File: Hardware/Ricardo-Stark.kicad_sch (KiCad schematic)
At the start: 54 parts, among them J1 RBUS, U1 ESP32-S3, Y1 R940000171

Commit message: updated sensors and other stuff
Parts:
- removed 3V3LED10: PURPLE_LED, LED_SMD:LED_0402_1005Metric, symbol Device:LED_Small
- removed 3V3LED2, 3V3LED3, 3V3LED4, 3V3LED8: BLUE_LED, LED_SMD:LED_0402_1005Metric, symbol Device:LED_Small
- removed 3V3LED5: ORANGE_LED, LED_SMD:LED_0402_1005Metric, symbol Device:LED_Small
- removed 3V3LED6: RED_LED, LED_SMD:LED_0402_1005Metric, symbol Device:LED_Small
- removed 3V3LED7: YELLOW_LED, LED_SMD:LED_0402_1005Metric, symbol Device:LED_Small
- removed 3V3LED9: GREEN_LED, LED_SMD:LED_0402_1005Metric, symbol Device:LED_Small
- removed JP31: SolderJumper_2_Open, iclr:SmallerSolderJP, symbol Jumper:SolderJumper_2_Open
- removed R11, R12, R13, R44: 470, Resistor_SMD:R_0402_1005Metric, symbol Device:R_Small
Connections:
- net GPIO37: no longer U1.42 (GPIO37)
- net GPIO38: no longer U1.43 (GPIO38)
- net GPIO39: no longer U1.44 (MTCK/JTAG/GPIO39)
- net GPIO40: no longer U1.45 (MTDO/JTAG/GPIO40)
- net GPIO41: no longer U1.47 (MTDI/JTAG/GPIO41)
- net GPIO42: no longer U1.48 (MTMS/JTAG/GPIO42)
- net SD1_CS: no longer U1.11 (GPIO6/ADC1_CH5)
- net SD1_DET: no longer U1.9 (GPIO4/ADC1_CH3)
- net SD_EN: no longer U1.10 (GPIO5/ADC1_CH4)
- net VSPI_MISO: no longer U1.14 (GPIO9/ADC1_CH8)
- net VSPI_MOSI: no longer U1.12 (GPIO7/ADC1_CH6)
- net VSPI_SCLK: no longer U1.13 (GPIO8/ADC1_CH7)
- net LEDC: no longer names the net of U1.28 (SPI_CS1/GPIO26)
- new net GPIO4: U1.9 (GPIO4/ADC1_CH3)
- new net GPIO5: U1.10 (GPIO5/ADC1_CH4)
- new net GPIO6: U1.11 (GPIO6/ADC1_CH5)
- new net GPIO7: U1.12 (GPIO7/ADC1_CH6)
- new net GPIO8: U1.13 (GPIO8/ADC1_CH7)
- new net GPIO9: U1.14 (GPIO9/ADC1_CH8)
- no-connect marks 14 -> 15
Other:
- sheet actuators renamed Actuators
- sheet buckC renamed ServoPower
- sheet pressure_sensor renamed Sensors
- added sheet Fuzzzze (Fuzzzze.kicad_sch)
- added sheet LEDs (LEDs.kicad_sch)
- note added: "Integrated SPI flash, don't use"

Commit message: rearranged comps
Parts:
- J1: footprint Connector_Molex:Molex_Mini-Fit_Jr_5566-06A_2x03_P4.20mm_Vertical -> Connector_Molex:Molex_Mini-Fit_Jr_5569-06A2_2x03_P4.20mm_Horizontal
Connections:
- net ADS_CS0: no longer U1.41 (GPIO36)
- net at R20.2: now also U1.42 (GPIO37); no longer U1.36 (SPICLK_N/GPIO48)
- net DRDY: no longer names the net of U1.40 (GPIO35)
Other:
- sheet Sensors ports: added ADS_DRDY, MISO, MOSI, SCLK, TC_CS, TC_DRDY, TC_FAULT; removed ADS_MISO, ADS_MOSI, ADS_SCLK, DRDY
- moved on the sheet: R20
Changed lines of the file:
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@@
 	(wire
 		(pts
-			(xy 212.09 83.82) (xy 220.98 83.82)
+			(xy 215.392 84.074) (xy 224.282 84.074)
 		)
 		(stroke
@@
 	(wire
 		(pts
-			(xy 212.09 81.28) (xy 220.98 81.28)
+			(xy 215.392 81.534) (xy 224.282 81.534)
 		)
 		(stroke
@@
 	(wire
 		(pts
-			(xy 212.09 76.2) (xy 220.98 76.2)
+			(xy 215.392 76.454) (xy 224.282 76.454)
 		)
 		(stroke
@@
 	(wire
 		(pts
-			(xy 212.09 78.74) (xy 220.98 78.74)
+			(xy 215.392 78.994) (xy 224.282 78.994)
 		)
 		(stroke
@@
 	(wire
 		(pts
-			(xy 212.09 86.36) (xy 220.98 86.36)
+			(xy 215.392 86.614) (xy 224.282 86.614)
 		)
 		(stroke
@@
 	)
 	(rectangle
-		(start 115.824 78.486)
+		(start 115.824 75.692)
 		(end 137.922 93.472)
 		(stroke
@@
 	)
 	(label "HSPI_MOSI"
-		(at 220.98 81.28 0)
+		(at 224.282 81.534 0)
 		(fields_autoplaced yes)
 		(effects
@@
 		)
 	)
+	(label "ADS_DRDY"
+		(at 186.182 80.518 180)
+		(fields_autoplaced yes)
+		(effects
+			(font
+				(size 1.27 1.27)
+			)
+			(justify right bottom)
+		)
+	)
 	(label "SD1_DET"
 		(at 48.006 103.378 180)
@@
 	)
 	(label "HSPI_MISO"
-		(at 220.98 83.82 0)
+		(at 224.282 84.074 0)
 		(fields_autoplaced yes)
 		(effects
@@
 	)
 	(label "HSPI_SCLK"
-		(at 220.98 78.74 0)
+		(at 224.282 78.994 0)
 		(fields_autoplaced yes)
 		(effects
@@
 		)
 	)
-	(label "DRDY"
-		(at 135.89 100.33 0)
-		(fields_autoplaced yes)
-		(effects
-			(font
-				(size 1.27 1.27)
-			)
-			(justify left bottom)
-		)
-	)
 	(label "CAN+"
 		(at 115.57 185.42 0)
@@
 	)
 	(label "ADS_CS0"
-		(at 220.98 86.36 0)
+		(at 224.282 86.614 0)
 		(fields_autoplaced yes)
 		(effects
@@
 	)
 	(label "ADS_CLK"
-		(at 140.97 115.57 0)
+		(at 140.97 105.41 0)
 		(fields_autoplaced yes)
 		(effects
@@
 		)
 	)
+	(label "TC_FAULT"
+		(at 186.182 77.47 180)
+		(fields_autoplaced yes)
+		(effects
+			(font
+				(size 1.27 1.27)
+			)
+			(justify right bottom)
+		)
+	)
 	(label "TXD"
 		(at 29.718 62.23 0)
@@
 		)
 	)
-	(label "DRDY"
-		(at 182.88 84.074 180)
+	(label "TC_DRDY"
+		(at 186.182 84.328 180)
+		(fields_autoplaced yes)
+		(effects
+			(font
+				(size 1.27 1.27)
+			)
+			(justify right bottom)
+		)
+	)
+	(label "TC_CS"
+		(at 186.182 86.614 180)
 		(fields_autoplaced yes)
 		(effects
@@
 		)
 	)
-	(label "ADS_CS0"
-		(at 135.89 102.87 0)
-		(fields_autoplaced yes)
-		(effects
-			(font
-				(size 1.27 1.27)
-			)
-			(justify left bottom)
-		)
-	)
 	(label "ADS_CLK"
-		(at 220.98 76.2 0)
+		(at 224.282 76.454 0)
 		(fields_autoplaced yes)
 		(effects
@@
 			)
 		)
-		(property "Footprint" "Connector_Molex:Molex_Mini-Fit_Jr_5566-06A_2x03_P4.20mm_Vertical"
+		(property "Footprint" "Connector_Molex:Molex_Mini-Fit_Jr_5569-06A2_2x03_P4.20mm_Horizontal"
 			(at 123.19 20.32 0)
 			(effects
@@
 	(symbol
 		(lib_id "Device:R_Small")
-		(at 138.43 115.57 270)
+		(at 138.43 105.41 270)
 		(mirror x)
 		(unit 1)
@@
 		(dnp no)
 		(property "Reference" "R20"
-			(at 138.43 113.538 90)
+			(at 138.43 103.378 90)
 			(effects
 				(font
@@
 		)
 		(property "Value" "54.9R"
-			(at 138.684 117.602 90)
+			(at 138.684 107.442 90)
 			(effects
 				(font
@@
 		)
 		(property "Footprint" "Resistor_SMD:R_0402_1005Metric"
-			(at 138.43 115.57 0)
+			(at 138.43 105.41 0)
 			(effects
 				(font
@@
 		)
 		(property "Datasheet" "~"
-			(at 138.43 115.57 0)
+			(at 138.43 105.41 0)
 			(effects
 				(font
@@
 		)
 		(property "Description" ""
-			(at 138.43 115.57 0)
+			(at 138.43 105.41 0)
 			(effects
 				(font
@@
 	)
 	(sheet
-		(at 182.88 73.66)
+		(at 186.182 73.914)
 		(size 29.21 13.97)
 		(fields_autoplaced yes)
@@
 		)
 		(property "Sheetname" "Sensors"
-			(at 182.88 72.9484 0)
+			(at 186.182 73.2024 0)
 			(effects
 				(font
@@
 		)
 		(property "Sheetfile" "pressure_sensor_sch.kicad_sch"
-			(at 182.88 88.2146 0)
+			(at 186.182 88.4686 0)
 			(effects
 				(font
@@
 		)
 		(pin "ADS_CLK" bidirectional
-			(at 212.09 76.2 0)
+			(at 215.392 76.454 0)
 			(effects
 				(font
@@
 			)
 		)
-		(pin "ADS_SCLK" bidirectional
-			(at 212.09 78.74 0)
+		(pin "ADS_CS0" bidirectional
+			(at 215.392 86.614 0)
 			(effects
 				(font
@@
 			)
 		)
-		(pin "ADS_MOSI" bidirectional
-			(at 212.09 81.28 0)
+		(pin "MOSI" input
+			(at 215.392 81.534 0)
 			(effects
 				(font
@@
 			)
 		)
-		(pin "ADS_MISO" bidirectional
-			(at 212.09 83.82 0)
+		(pin "MISO" output
+			(at 215.392 84.074 0)
 			(effects
 				(font
@@
 			)
 		)
-		(pin "ADS_CS0" bidirectional
-			(at 212.09 86.36 0)
+		(pin "ADS_DRDY" bidirectional
+			(at 186.182 80.518 180)
+			(effects
+				(font
+					(size 1.27 1.27)
+				)
+				(justify left)
+			)
+		)
+		(pin "SCLK" bidirectional
+			(at 215.392 78.994 0)
 			(effects
 				(font
@@
 			)
 		)
-		(pin "DRDY" bidirectional
-			(at 182.88 84.074 180)
+		(pin "TC_FAULT" output
+			(at 186.182 77.47 180)
+			(effects
+				(font
+					(size 1.27 1.27)
+				)
+				(justify left)
+			)
+		)
+		(pin "TC_CS" input
+			(at 186.182 86.614 180)
+			(effects
+				(font
+					(size 1.27 1.27)
+				)
+				(justify left)
+			)
+		)
+		(pin "TC_DRDY" output
+			(at 186.182 84.328 180)
 			(effects
 				(font

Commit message: Finished Boosts and Sensors
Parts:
- renumbered R20 to R91
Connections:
- net ADS_CS0: now also U1.41 (GPIO36)
- net ADS_DRDY: now also U1.40 (GPIO35)
- net HSPI_MISO: now also U1.37 (SPICLK_P/GPIO47); no longer U1.38 (GPIO33)
- net HSPI_MOSI: now also U1.36 (SPICLK_N/GPIO48); no longer U1.37 (SPICLK_P/GPIO47)
- net HSPI_SCLK: now also U1.38 (GPIO33); no longer U1.39 (GPIO34)
- net TC_CS: now also U1.39 (GPIO34)

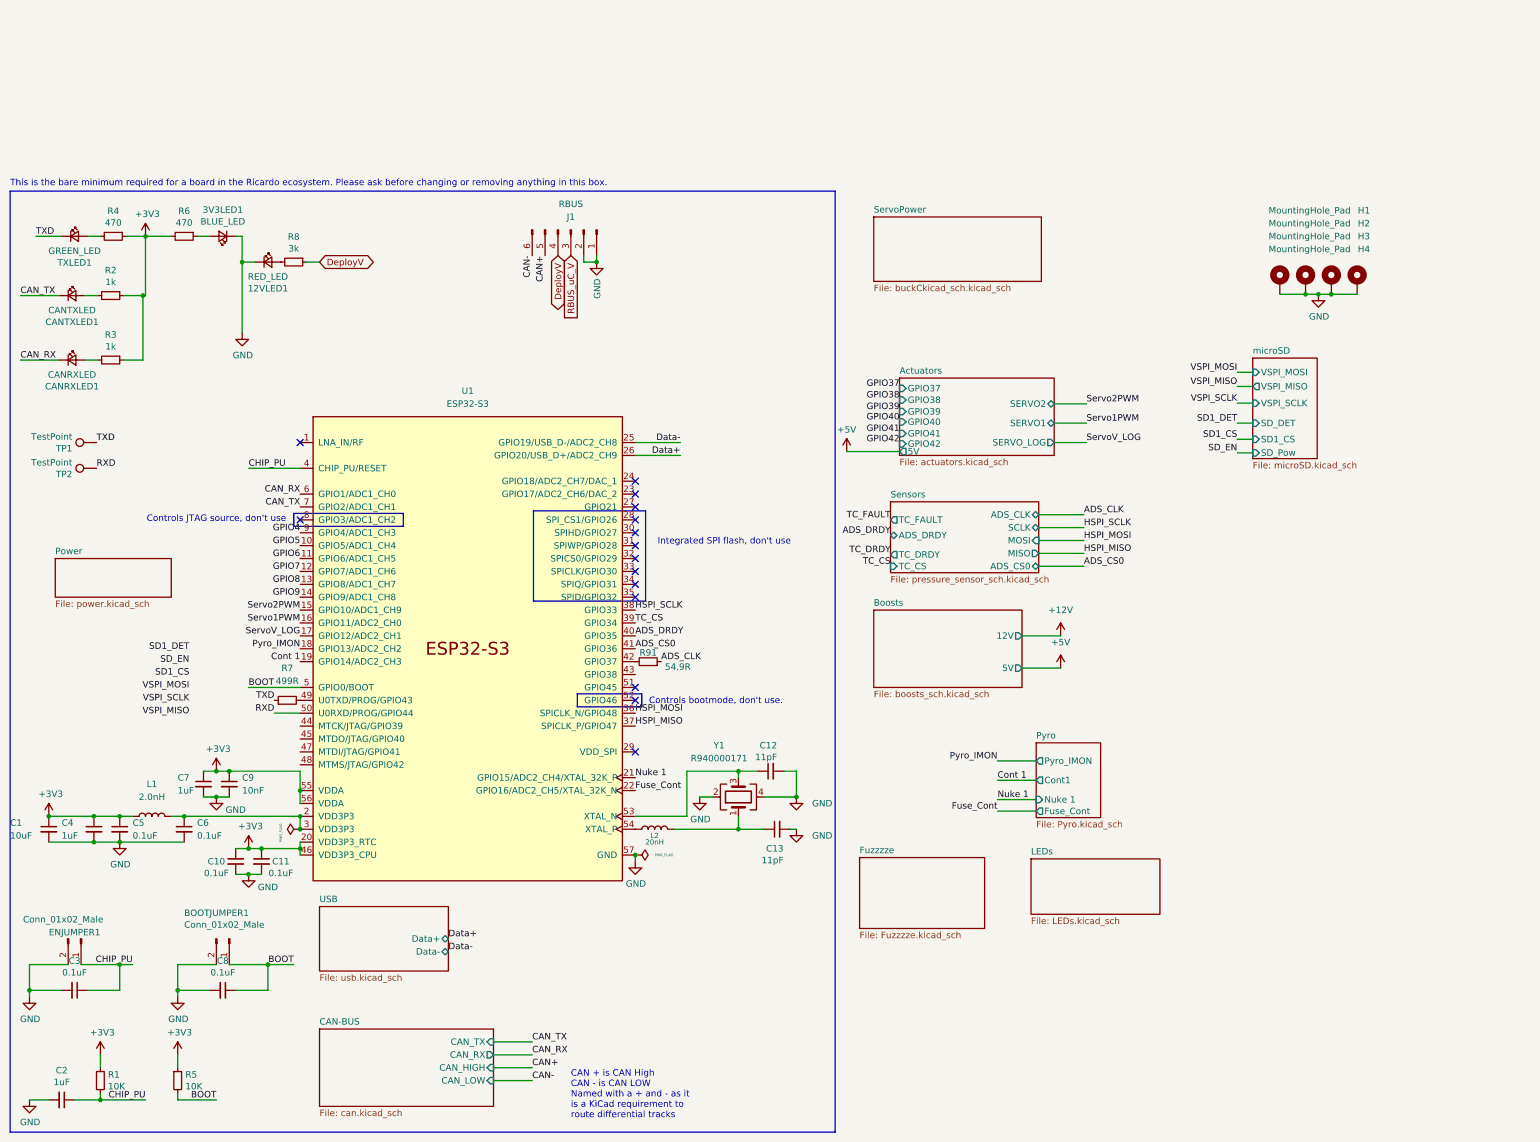
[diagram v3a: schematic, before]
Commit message: Updated SD card, GPIOs, CAN, Power section
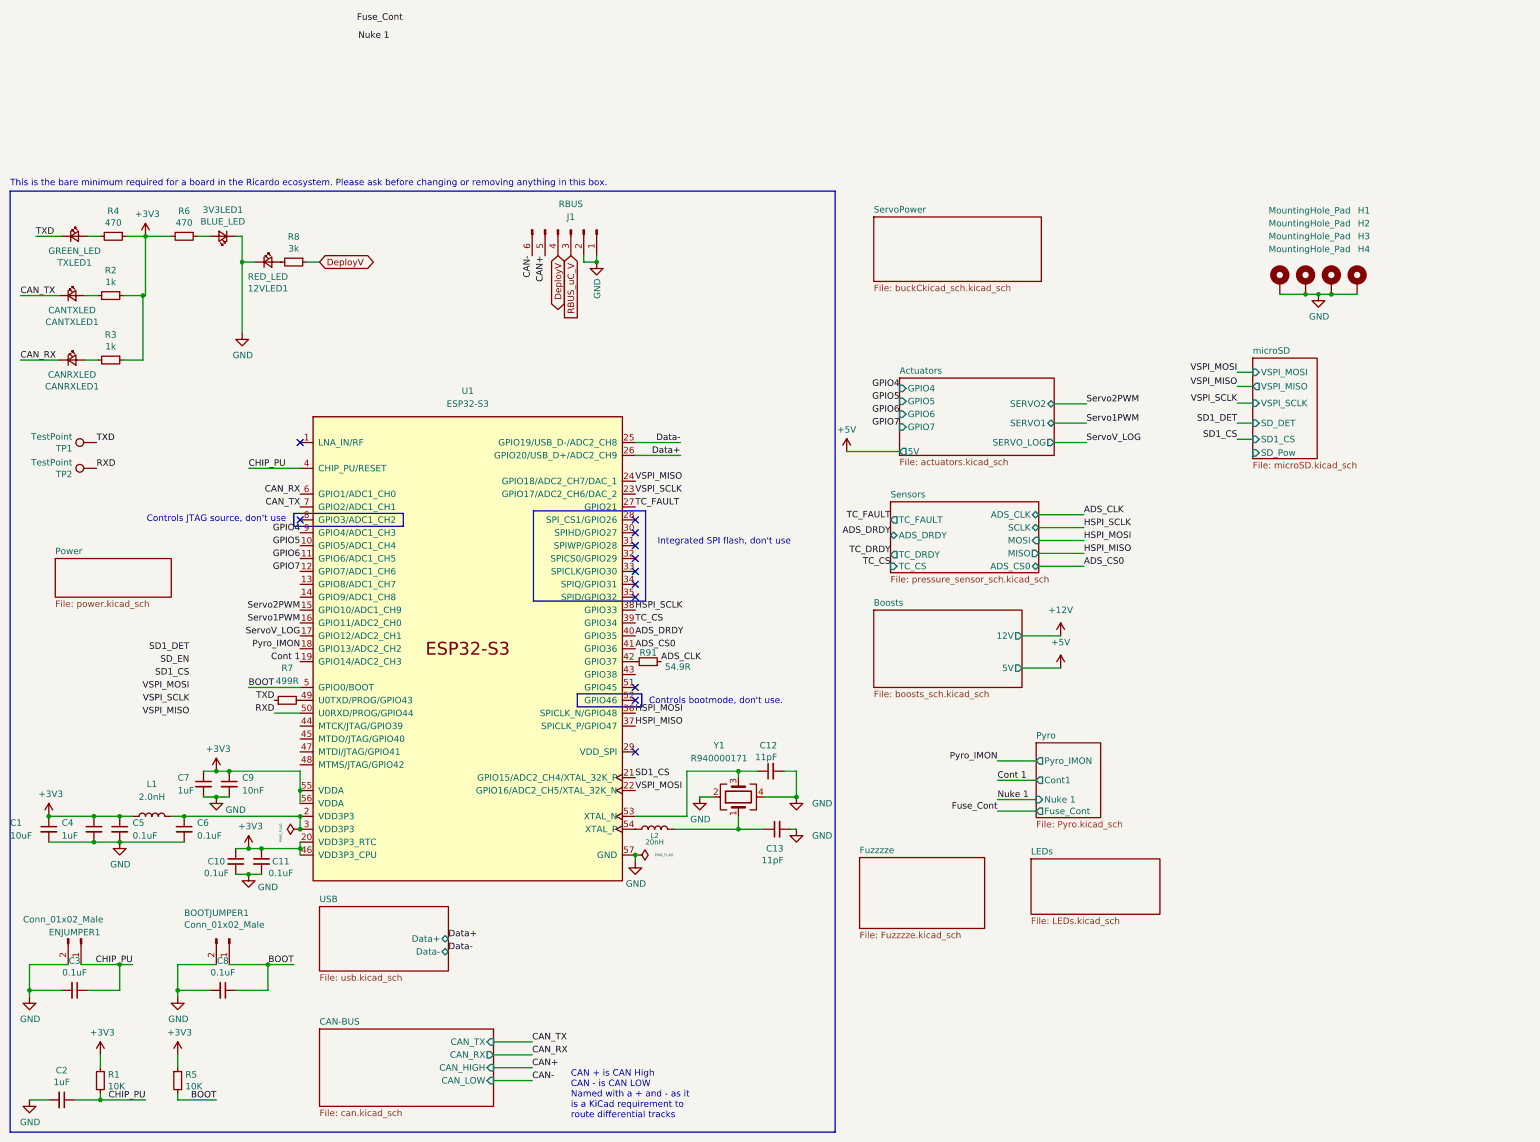
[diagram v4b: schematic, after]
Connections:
- net Fuse_Cont: no longer U1.22 (GPIO16/ADC2_CH5/XTAL_32K_N)
- net Nuke 1: no longer U1.21 (GPIO15/ADC2_CH4/XTAL_32K_P)
- net SD1_CS: now also U1.21 (GPIO15/ADC2_CH4/XTAL_32K_P)
- net TC_FAULT: now also U1.27 (GPIO21)
- net VSPI_MISO: now also U1.24 (GPIO18/ADC2_CH7/DAC_1)
- net VSPI_MOSI: now also U1.22 (GPIO16/ADC2_CH5/XTAL_32K_N)
- net VSPI_SCLK: now also U1.23 (GPIO17/ADC2_CH6/DAC_2)
- net GPIO8: no longer names the net of U1.13 (GPIO8/ADC1_CH7)
- net GPIO9: no longer names the net of U1.14 (GPIO9/ADC1_CH8)
- no-connect marks 15 -> 12
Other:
- sheet Actuators ports: added GPIO4, GPIO5, GPIO6, GPIO7; removed GPIO37, GPIO38, GPIO39, GPIO40, GPIO41, GPIO42
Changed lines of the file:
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@@
 	)
 	(no_connect
-		(at 135.89 69.85)
-	)
-	(no_connect
 		(at 135.89 82.55)
 	)
 	(no_connect
-		(at 135.89 72.39)
-	)
-	(no_connect
 		(at 135.89 110.49)
 	)
@@
 	)
 	(no_connect
-		(at 135.89 74.93)
-	)
-	(no_connect
 		(at 135.89 87.63)
 	)
@@
 	(wire
 		(pts
-			(xy 254.508 64.262) (xy 257.556 64.262)
-		)
-		(stroke
-			(width 0)
-			(type default)
-		)
-	)
-	(wire
-		(pts
 			(xy 148.59 132.08) (xy 151.13 132.08)
 		)
@@
 		)
 	)
+	(label "GPIO5"
+		(at 187.96 54.102 180)
+		(effects
+			(font
+				(size 1.27 1.27)
+			)
+			(justify right bottom)
+		)
+	)
+	(label "GPIO4"
+		(at 187.96 51.562 180)
+		(effects
+			(font
+				(size 1.27 1.27)
+			)
+			(justify right bottom)
+		)
+	)
+	(label "VSPI_MISO"
+		(at 135.89 69.85 0)
+		(effects
+			(font
+				(size 1.27 1.27)
+			)
+			(justify left bottom)
+		)
+	)
 	(label "HSPI_MOSI"
 		(at 224.282 81.534 0)
@@
 		)
 	)
-	(label "GPIO38"
-		(at 187.96 53.848 180)
-		(effects
-			(font
-				(size 1.27 1.27)
-			)
-			(justify right bottom)
-		)
-	)
 	(label "HSPI_MISO"
 		(at 224.282 84.074 0)
@@
 		)
 	)
-	(label "GPIO37"
-		(at 187.96 51.562 180)
-		(effects
-			(font
-				(size 1.27 1.27)
-			)
-			(justify right bottom)
-		)
-	)
 	(label "HSPI_SCLK"
 		(at 224.282 78.994 0)
@@
 		)
 	)
-	(label "GPIO8"
-		(at 69.85 90.17 180)
-		(effects
-			(font
-				(size 1.27 1.27)
-			)
-			(justify right bottom)
-		)
-	)
 	(label "VSPI_SCLK"
 		(at 48.006 113.538 180)
@@
 		)
 	)
-	(label "SD_EN"
-		(at 254.508 64.262 180)
-		(effects
-			(font
-				(size 1.27 1.27)
-			)
-			(justify right bottom)
-		)
-	)
 	(label "SD1_CS"
 		(at 48.006 108.458 180)
@@
 		)
 	)
+	(label "GPIO7"
+		(at 187.96 59.182 180)
+		(effects
+			(font
+				(size 1.27 1.27)
+			)
+			(justify right bottom)
+		)
+	)
 	(label "Data-"
 		(at 99.06 162.56 0)
@@
 	)
 	(label "Fuse_Cont"
-		(at 135.89 130.81 0)
+		(at 81.026 -20.574 0)
 		(effects
 			(font
@@
 		)
 	)
+	(label "TC_FAULT"
+		(at 135.89 74.93 0)
+		(effects
+			(font
+				(size 1.27 1.27)
+			)
+			(justify left bottom)
+		)
+	)
 	(label "TC_CS"
 		(at 186.182 86.614 180)
@@
 		)
 	)
-	(label "GPIO9"
-		(at 69.85 92.71 180)
-		(effects
-			(font
-				(size 1.27 1.27)
-			)
-			(justify right bottom)
-		)
-	)
 	(label "GPIO7"
 		(at 69.85 87.63 180)
@@
 		)
 	)
-	(label "GPIO42"
-		(at 187.96 62.484 180)
+	(label "SD1_CS"
+		(at 135.89 128.27 0)
 		(effects
 			(font
 				(size 1.27 1.27)
 			)
-			(justify right bottom)
+			(justify left bottom)
 		)
 	)
@@
 	)
 	(label "Nuke 1"
-		(at 135.89 128.27 0)
+		(at 81.28 -17.018 0)
 		(effects
 			(font
@@
 		)
 	)
-	(label "GPIO39"
-		(at 187.96 56.134 180)
+	(label "CHIP_PU"
+		(at 59.69 67.31 0)
 		(effects
 			(font
 				(size 1.27 1.27)
 			)
-			(justify right bottom)
+			(justify left bottom)
 		)
 	)
-	(label "CHIP_PU"
-		(at 59.69 67.31 0)
+	(label "VSPI_MISO"
+		(at 254.508 51.181 180)
 		(effects
 			(font
 				(size 1.27 1.27)
 			)
-			(justify left bottom)
+			(justify right bottom)
 		)
 	)
-	(label "VSPI_MISO"
-		(at 254.508 51.181 180)
+	(label "GPIO6"
+		(at 187.96 56.642 180)
 		(effects
 			(font
@@
 		)
 	)
-	(label "GPIO41"
-		(at 187.96 60.452 180)
+	(label "VSPI_MOSI"
+		(at 135.89 130.81 0)
 		(effects
 			(font
 				(size 1.27 1.27)
 			)
-			(justify right bottom)
+			(justify left bottom)
 		)
 	)
@@
 		)
 	)
-	(label "GPIO40"
-		(at 187.96 58.166 180)
+	(label "HSPI_MISO"
+		(at 135.89 118.11 0)
 		(effects
 			(font
 				(size 1.27 1.27)
 			)
-			(justify right bottom)
+			(justify left bottom)
 		)
 	)
-	(label "HSPI_MISO"
-		(at 135.89 118.11 0)
+	(label "VSPI_SCLK"
+		(at 135.89 72.39 0)
 		(effects
 			(font
@@
 			)
 		)
-		(pin "GPIO38" input
-			(at 187.96 53.848 180)
-			(effects
-				(font
-					(size 1.27 1.27)
-				)
-				(justify left)
-			)
-		)
-		(pin "GPIO37" input
+		(pin "GPIO4" input
 			(at 187.96 51.562 180)
 			(effects
@@
 			)
 		)
-		(pin "GPIO41" input
-			(at 187.96 60.452 180)
-			(effects
-				(font
-					(size 1.27 1.27)
-				)
-				(justify left)
-			)
-		)
-		(pin "GPIO39" input
-			(at 187.96 56.134 180)
+		(pin "GPIO5" input
+			(at 187.96 54.102 180)
 			(effects
 				(font
@@
 			)
 		)
-		(pin "GPIO40" input
-			(at 187.96 58.166 180)
+		(pin "GPIO6" input
+			(at 187.96 56.642 180)
 			(effects
 				(font
@@
 			)
 		)
-		(pin "GPIO42" input
-			(at 187.96 62.484 180)
+		(pin "GPIO7" input
+			(at 187.96 59.182 180)
 			(effects
 				(font
